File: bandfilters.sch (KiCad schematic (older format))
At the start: 25 parts, among them K1 BAND3_IN, K2 BAND2_IN, K3 BAND1_IN, K4 BAND3_OUT, K5 BAND2_OUT, K6 BAND1_OUT

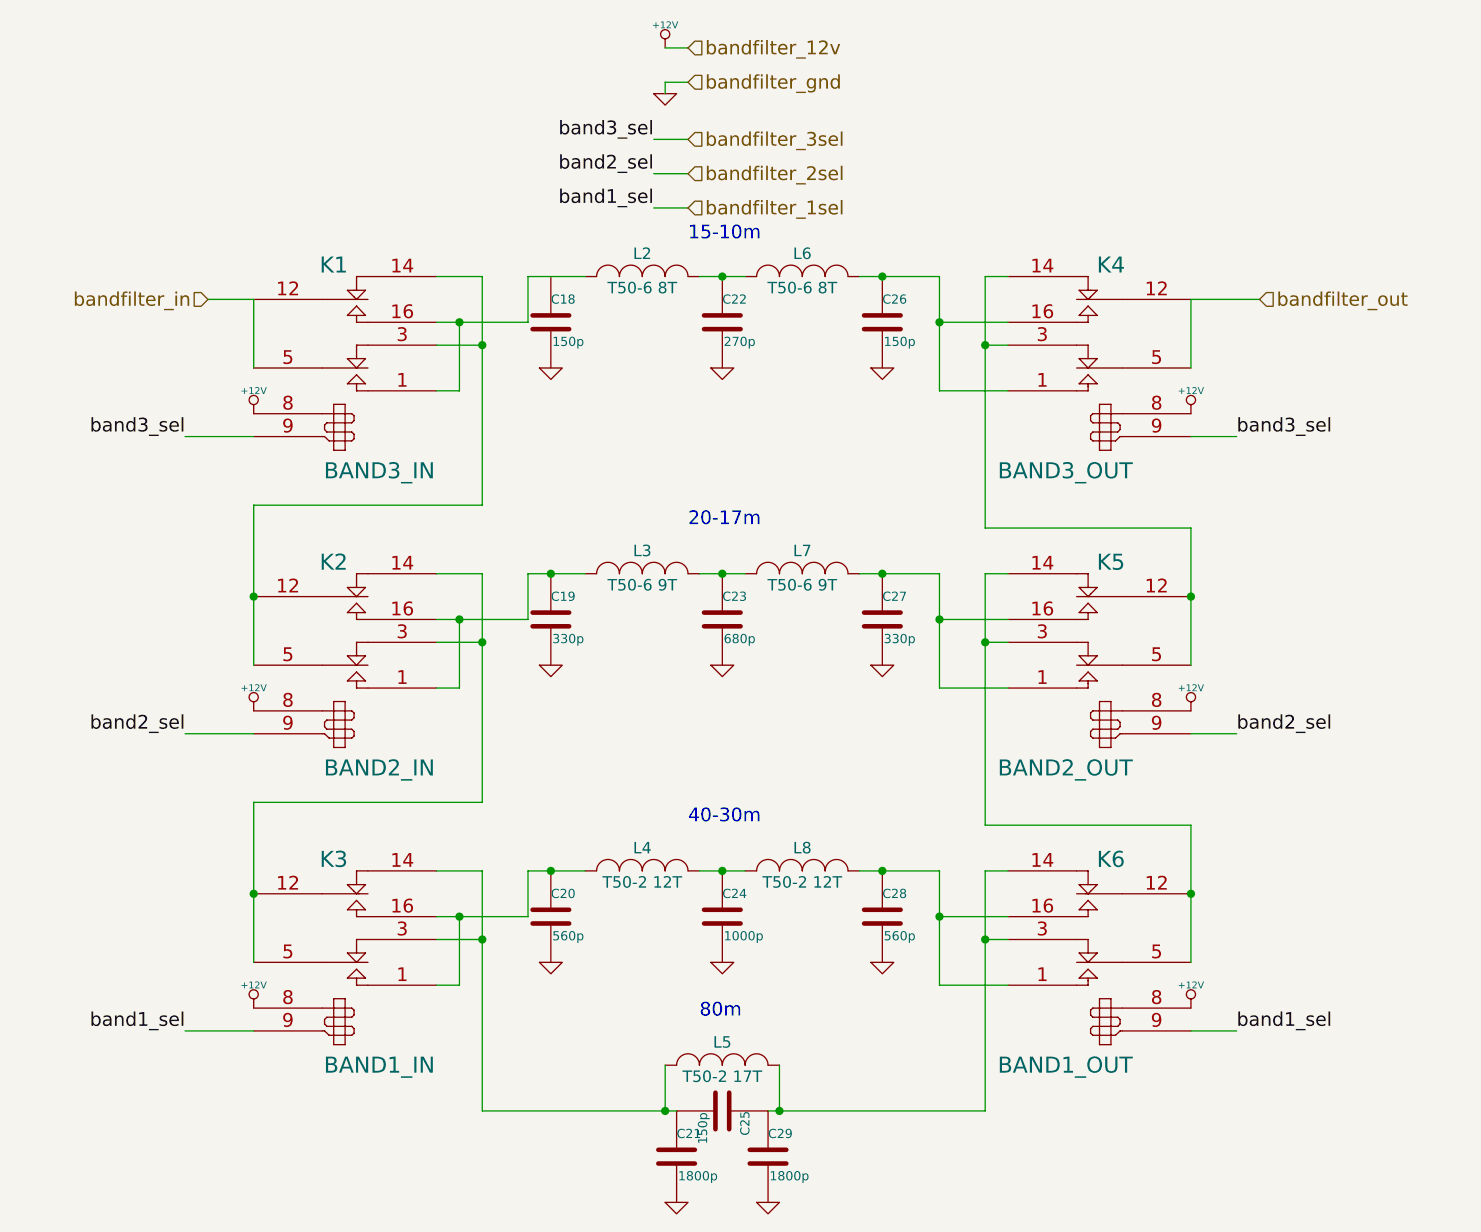
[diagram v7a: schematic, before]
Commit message: All layed out
Several net errors fixed, and some mcu pins reassigned for better layout.
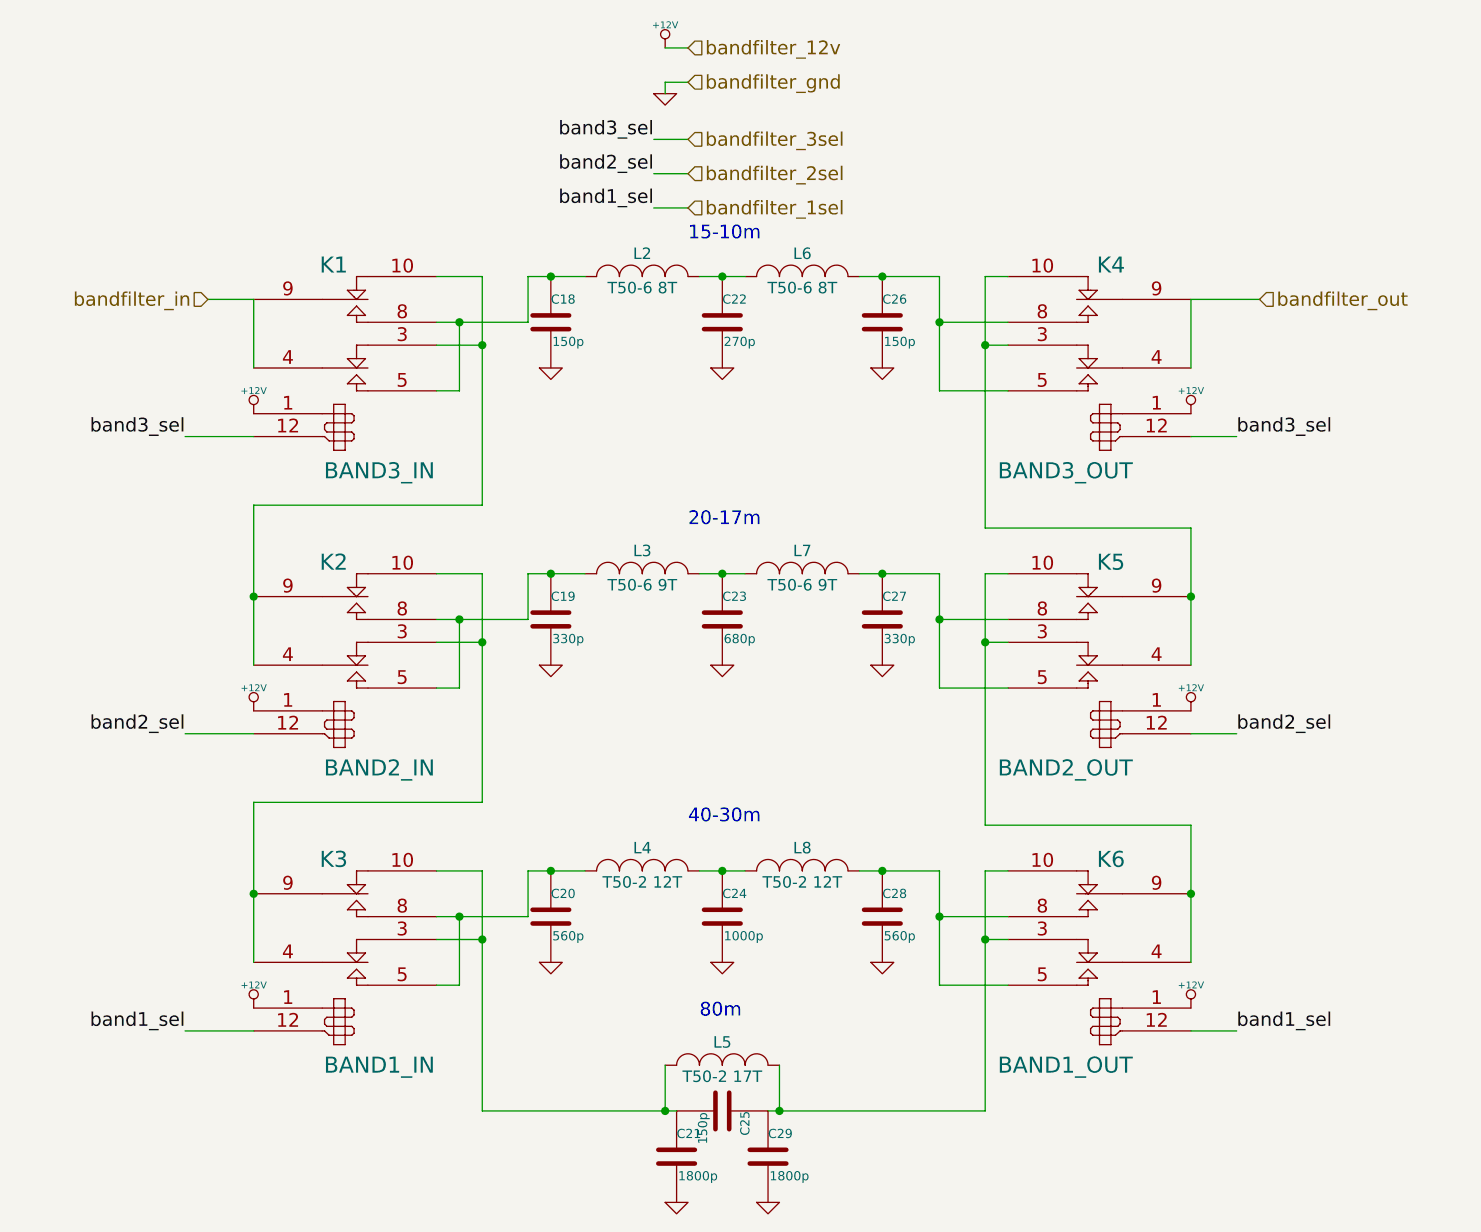
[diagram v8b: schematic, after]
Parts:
- removed K1: BAND3_IN, nu9j-footprints:EC2-12NU, symbol RELAY_2RT
- removed K2: BAND2_IN, nu9j-footprints:EC2-12NU, symbol RELAY_2RT
- removed K3: BAND1_IN, nu9j-footprints:EC2-12NU, symbol RELAY_2RT
- removed K4: BAND3_OUT, nu9j-footprints:EC2-12NU, symbol RELAY_2RT
- removed K5: BAND2_OUT, nu9j-footprints:EC2-12NU, symbol RELAY_2RT
- removed K6: BAND1_OUT, nu9j-footprints:EC2-12NU, symbol RELAY_2RT
- added K1: BAND3_IN, symbol RELAY_2RT-KEMET
- added K2: BAND2_IN, symbol RELAY_2RT-KEMET
- added K3: BAND1_IN, symbol RELAY_2RT-KEMET
- added K4: BAND3_OUT, symbol RELAY_2RT-KEMET
- added K5: BAND2_OUT, symbol RELAY_2RT-KEMET
- added K6: BAND1_OUT, symbol RELAY_2RT-KEMET
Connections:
- net +12V: now also K1.1, K2.1, K3.1, K4.1, K5.1, K6.1
- net bandfilter_1sel: now also K3.12, K6.12
- net bandfilter_2sel: now also K2.12, K5.12
- net bandfilter_3sel: now also K1.12, K4.12
- net bandfilter_in: now also K1.4, K1.9
- net bandfilter_out: now also K4.4, K4.9
- net at C18.1: now also L2.1, K1.5, K1.8
- net at C26.1, L6.2: now also K4.5, K4.8
- net at C19.1, L3.1: now also K2.5, K2.8
- net at C27.1, L7.2: now also K5.5, K5.8
- net at C20.1, L4.1: now also K3.5, K3.8
- net at C28.1, L8.2: now also K6.5, K6.8
- net at C21.1, C25.2, L5.1: now also K3.10, K3.3 (R1)
- net at C25.1, C29.1, L5.2: now also K6.10, K6.3 (R1)
- new net: K1.10, K1.3 (R1), K2.4, K2.9
- new net: K2.10, K2.3 (R1), K3.4, K3.9
- new net: K5.10, K5.3 (R1), K6.4, K6.9
- new net: K4.10, K4.3 (R1), K5.4, K5.9
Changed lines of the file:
@@
 Text Notes 5700 2000 0    60   ~ 0
 15-10m
+Connection ~ 5100 2150
 $Comp
-L RELAY_2RT K1
-U 1 1 547A7FD1
+L RELAY_2RT-KEMET K1
+U 1 1 54848992
 P 4200 2500
 F 0 "K1" H 4150 2900 70  0000 C CNN
 F 1 "BAND3_IN" H 4350 2000 70  0000 C CNN
-F 2 "nu9j-footprints:EC2-12NU" H 4200 2500 60  0001 C CNN
+F 2 "" H 4200 2500 60  0000 C CNN
 F 3 "" H 4200 2500 60  0000 C CNN
 	1    4200 2500
@@
 $EndComp
 $Comp
-L RELAY_2RT K2
-U 1 1 547A8128
+L RELAY_2RT-KEMET K2
+U 1 1 548489DD
 P 4200 3800
 F 0 "K2" H 4150 4200 70  0000 C CNN
 F 1 "BAND2_IN" H 4350 3300 70  0000 C CNN
-F 2 "nu9j-footprints:EC2-12NU" H 4200 3800 60  0001 C CNN
+F 2 "" H 4200 3800 60  0000 C CNN
 F 3 "" H 4200 3800 60  0000 C CNN
 	1    4200 3800
@@
 $EndComp
 $Comp
-L RELAY_2RT K3
-U 1 1 547A818C
+L RELAY_2RT-KEMET K3
+U 1 1 54848A30
 P 4200 5100
 F 0 "K3" H 4150 5500 70  0000 C CNN
 F 1 "BAND1_IN" H 4350 4600 70  0000 C CNN
-F 2 "nu9j-footprints:EC2-12NU" H 4200 5100 60  0001 C CNN
+F 2 "" H 4200 5100 60  0000 C CNN
 F 3 "" H 4200 5100 60  0000 C CNN
 	1    4200 5100
@@
 $EndComp
 $Comp
-L RELAY_2RT K6
-U 1 1 547A822E
+L RELAY_2RT-KEMET K6
+U 1 1 54848AAA
 P 7500 5100
 F 0 "K6" H 7450 5500 70  0000 C CNN
 F 1 "BAND1_OUT" H 7650 4600 70  0000 C CNN
-F 2 "nu9j-footprints:EC2-12NU" H 7500 5100 60  0001 C CNN
+F 2 "" H 7500 5100 60  0000 C CNN
 F 3 "" H 7500 5100 60  0000 C CNN
 	1    7500 5100
@@
 $EndComp
 $Comp
-L RELAY_2RT K5
-U 1 1 547A834D
+L RELAY_2RT-KEMET K4
+U 1 1 54849468
+P 7500 2500
+F 0 "K4" H 7450 2900 70  0000 C CNN
+F 1 "BAND3_OUT" H 7650 2000 70  0000 C CNN
+F 2 "" H 7500 2500 60  0000 C CNN
+F 3 "" H 7500 2500 60  0000 C CNN
+	1    7500 2500
+	-1   0    0    -1
+$EndComp
+$Comp
+L RELAY_2RT-KEMET K5
+U 1 1 548494DE
 P 7500 3800
 F 0 "K5" H 7450 4200 70  0000 C CNN
 F 1 "BAND2_OUT" H 7650 3300 70  0000 C CNN
-F 2 "nu9j-footprints:EC2-12NU" H 7500 3800 60  0001 C CNN
+F 2 "" H 7500 3800 60  0000 C CNN
 F 3 "" H 7500 3800 60  0000 C CNN
 	1    7500 3800
 	-1   0    0    -1
 $EndComp
-$Comp
-L RELAY_2RT K4
-U 1 1 547A83AD
-P 7500 2500
-F 0 "K4" H 7450 2900 70  0000 C CNN
-F 1 "BAND3_OUT" H 7650 2000 70  0000 C CNN
-F 2 "nu9j-footprints:EC2-12NU" H 7500 2500 60  0001 C CNN
-F 3 "" H 7500 2500 60  0000 C CNN
-	1    7500 2500
-	-1   0    0    -1
-$EndComp
